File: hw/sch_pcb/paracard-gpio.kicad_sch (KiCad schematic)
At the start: 1 part, among them P1 BTH-030-01-F-D-A

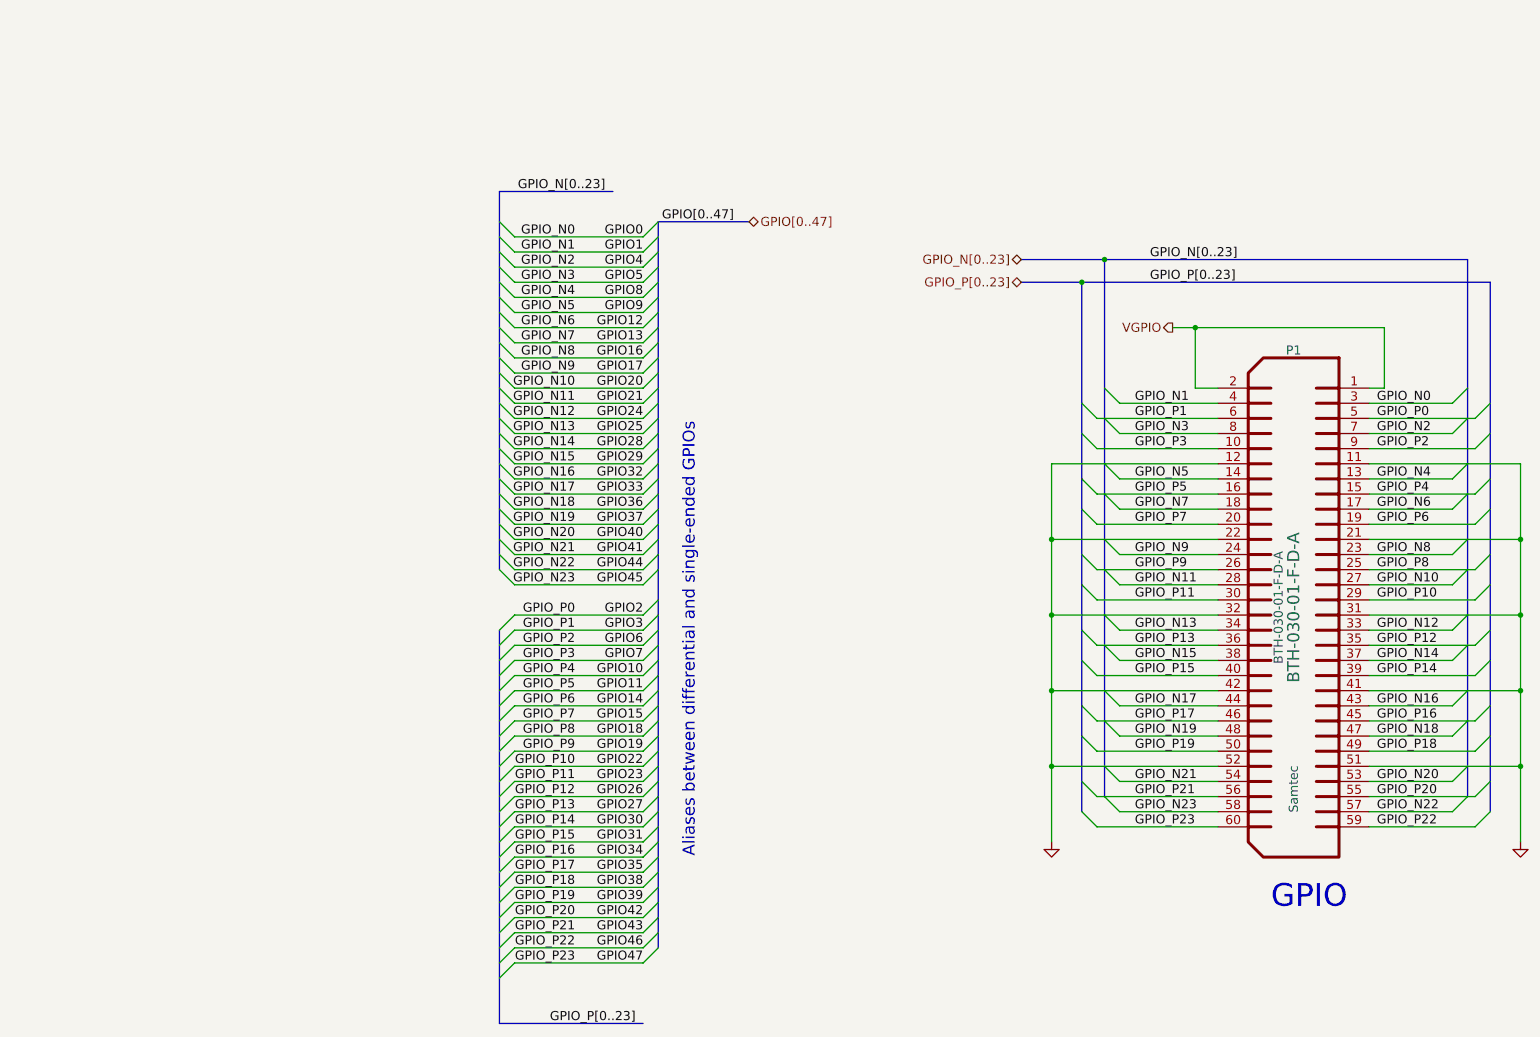
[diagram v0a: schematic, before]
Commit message: Update and improve documentation.
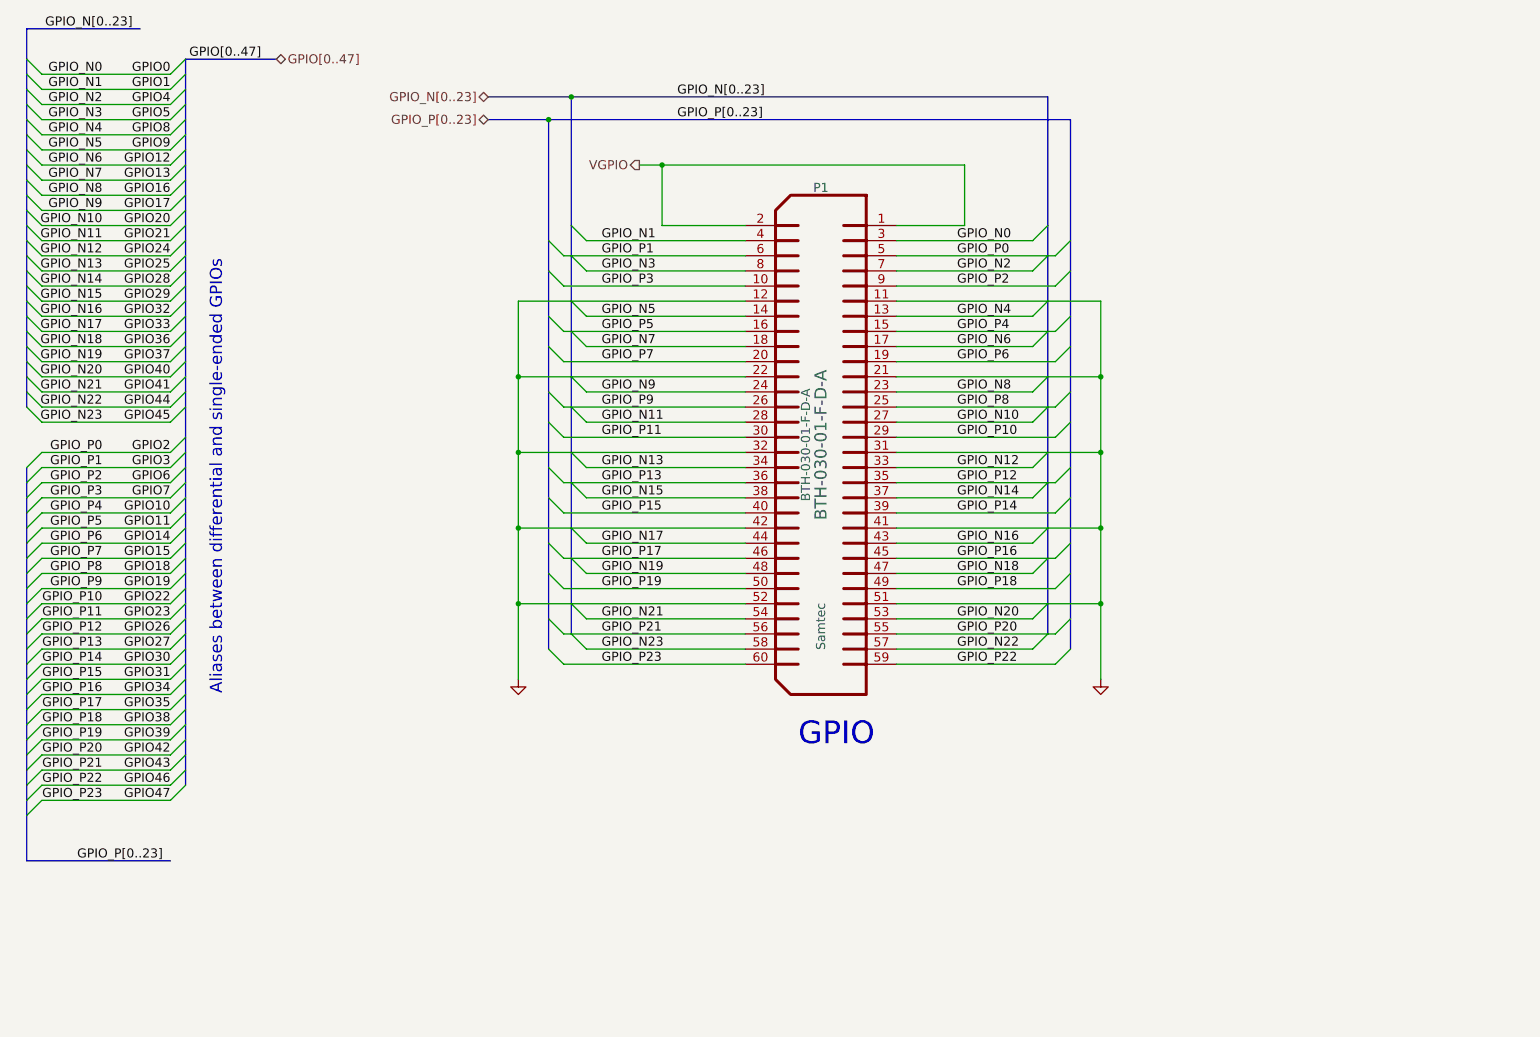
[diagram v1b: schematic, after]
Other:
- moved on the sheet: P1

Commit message: Update schematics. Preparation to resolve #2.
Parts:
- P1: footprint CONN_SAMTEC_BTH_60 -> Mlab_CON:SAMTEC-BTH-030-01-X-D-A; symbol adapteva_kicad:CONN_SAMTEC_BTH_60 -> MLAB_CONNECTORS:CONN_SAMTEC_BTH_030
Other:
- company: ORBISYS www.orbisys.sk -> MLAB.cz
- title: MPPB01A -> MPPB01B
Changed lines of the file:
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@@
   (paper "A4")
   (title_block
-    (title "MPPB01A")
-    (date "09 May 2014")
-    (rev "REV 0.1")
-    (company "ORBISYS www.orbisys.sk")
+    (title "MPPB01B")
+    (date "2022-03-24")
+    (company "MLAB.cz")
     (comment 1 "VERSION 1")
     (comment 2 "Paralella reduction board")
-    (comment 3 "Maksim Rezenov, Jakub kakona")
+    (comment 3 "Maksim Rezenov, Jakub Kakona")
   )
   (junction (at 233.045 104.775) (diameter 0) (color 0 0 0 0)
@@
     (pin "1")
   )
-  (symbol (lib_id "adapteva_kicad:CONN_SAMTEC_BTH_60") (at 186.055 103.505 0) (unit 1)
+  (symbol (lib_id "MLAB_CONNECTORS:CONN_SAMTEC_BTH_030") (at 186.055 103.505 0) (unit 1)
     (in_bom yes) (on_board yes)
     (property "Reference" "P1" (id 0) (at 186.055 60.325 0)
@@
       (effects (font (size 1.524 1.524)))
     )
-    (property "Footprint" "CONN_SAMTEC_BTH_60" (id 2) (at 188.595 103.505 90)
+    (property "Footprint" "Mlab_CON:SAMTEC-BTH-030-01-X-D-A" (id 2) (at 188.595 103.505 90)
       (effects (font (size 1.524 1.524)) hide)
     )
-    (property "Datasheet" "" (id 3) (at 188.595 80.645 0)
+    (property "Datasheet" "https://cz.mouser.com/datasheet/2/527/bth-2498158.pdf" (id 3) (at 188.595 80.645 0)
       (effects (font (size 1.524 1.524)) hide)
     )

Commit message: Priprava pro osazeni
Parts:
- P1: value BTH-030-01-F-D-A -> (none); footprint Mlab_CON:SAMTEC-BTH-030-01-X-D-A -> (none); UST_ID (none) -> 628e4f00243ef5997b12f43c
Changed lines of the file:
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@@
       (effects (font (size 1.524 1.524)))
     )
-    (property "Value" "BTH-030-01-F-D-A" (id 1) (at 183.515 103.505 90)
+    (property "Value" "" (id 1) (at 183.515 103.505 90)
       (effects (font (size 1.524 1.524)))
     )
-    (property "Footprint" "Mlab_CON:SAMTEC-BTH-030-01-X-D-A" (id 2) (at 188.595 103.505 90)
+    (property "Footprint" "" (id 2) (at 188.595 103.505 90)
       (effects (font (size 1.524 1.524)) hide)
     )
@@
       (effects (font (size 1.524 1.524)))
     )
+    (property "UST_ID" "628e4f00243ef5997b12f43c" (id 6) (at 186.055 103.505 0)
+      (effects (font (size 1.27 1.27)) hide)
+    )
     (pin "1")

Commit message: update assets, save as 7
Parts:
- P1: value (none) -> BTH-030-01-F-D-A; footprint (none) -> Mlab_CON:SAMTEC-BTH-030-01-X-D-A
